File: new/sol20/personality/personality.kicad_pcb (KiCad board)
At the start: 2 copper layers, 44.4 x 96.5 mm, 8 parts, among them J1 Personality-connector, U1 74LS08, U2 28C256

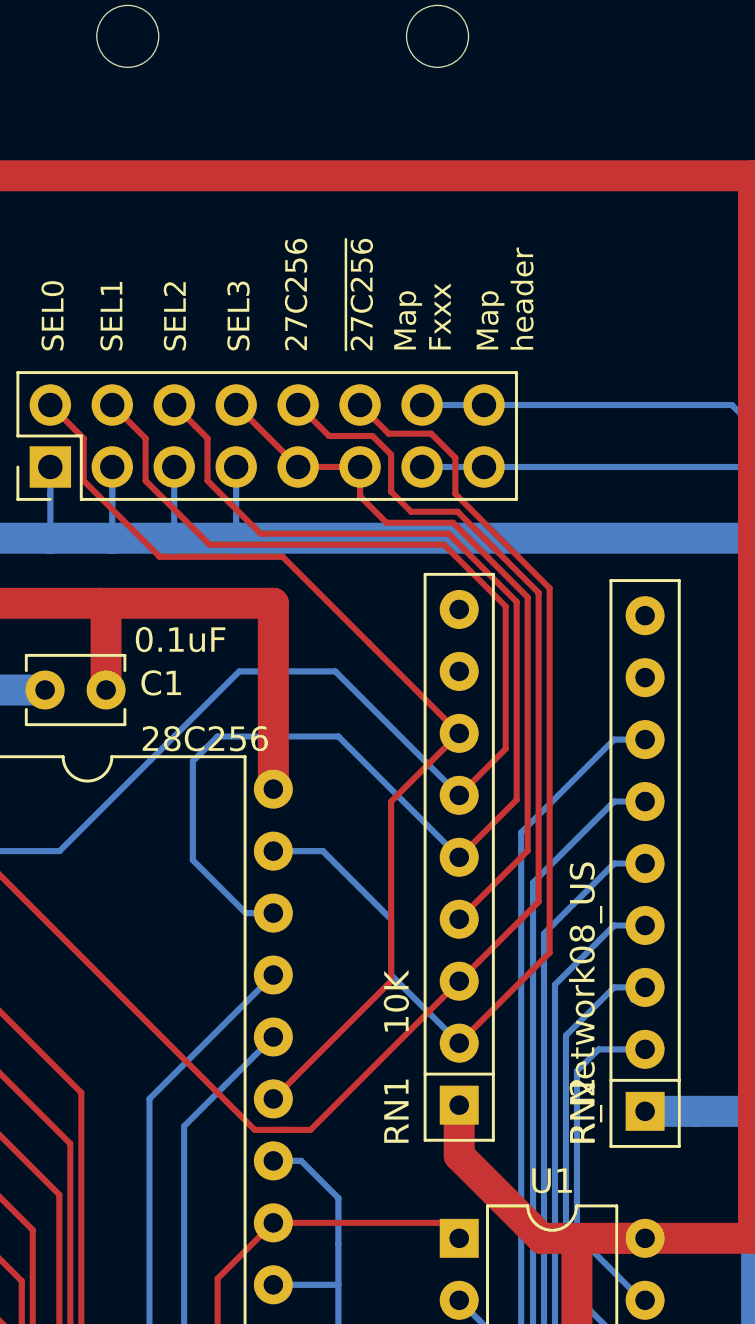
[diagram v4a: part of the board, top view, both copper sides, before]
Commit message: - fixed silk screen error (wrong string for RN2 value) - removed unnecessary pullup on the SEL3 jumper - renamed ~27C256 jumper to 27C256
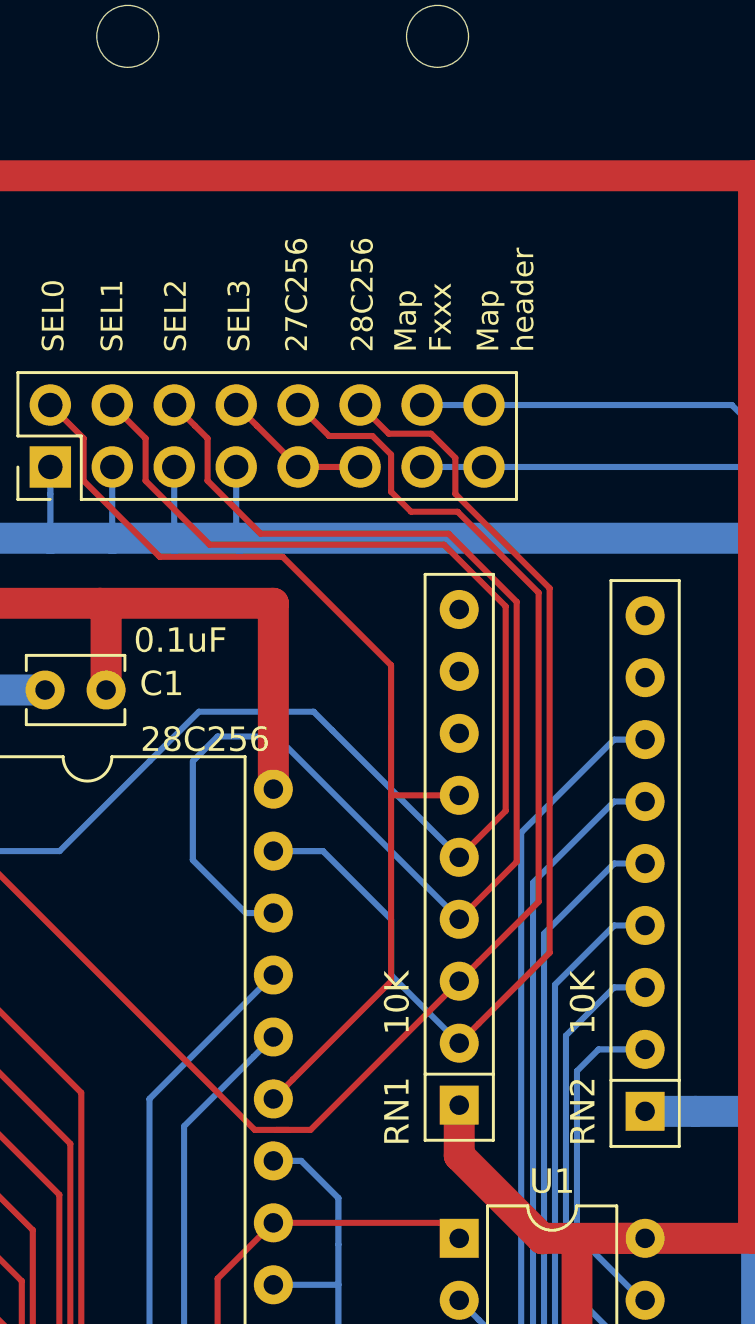
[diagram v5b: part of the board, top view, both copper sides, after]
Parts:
- RN2: value R_Network08_US -> 10K
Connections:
- RN1 pad 4: /BKSEL_3 -> /BKSEL_2
- RN1 pad 5: /BKSEL_2 -> /BKSEL_1
- RN1 pad 6: /BKSEL_1 -> /BKSEL_0
- RN1 pad 7: /BKSEL_0 -> Net-(RN1-Pad7)
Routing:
- net /BKSEL_3: track 30.3 -> 6.13 mm
- net /BKSEL_2: track 51.5 -> 55.1 mm
- net /BKSEL_1: track 57.1 -> 59.3 mm
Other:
- board text added: "28C256"
- board text removed: "~27C256"
